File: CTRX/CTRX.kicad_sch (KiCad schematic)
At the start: 3 parts, among them J1 USB_B_Micro, U1 nRF52820-QDxx, U2 NRF21540-QDAA-R7

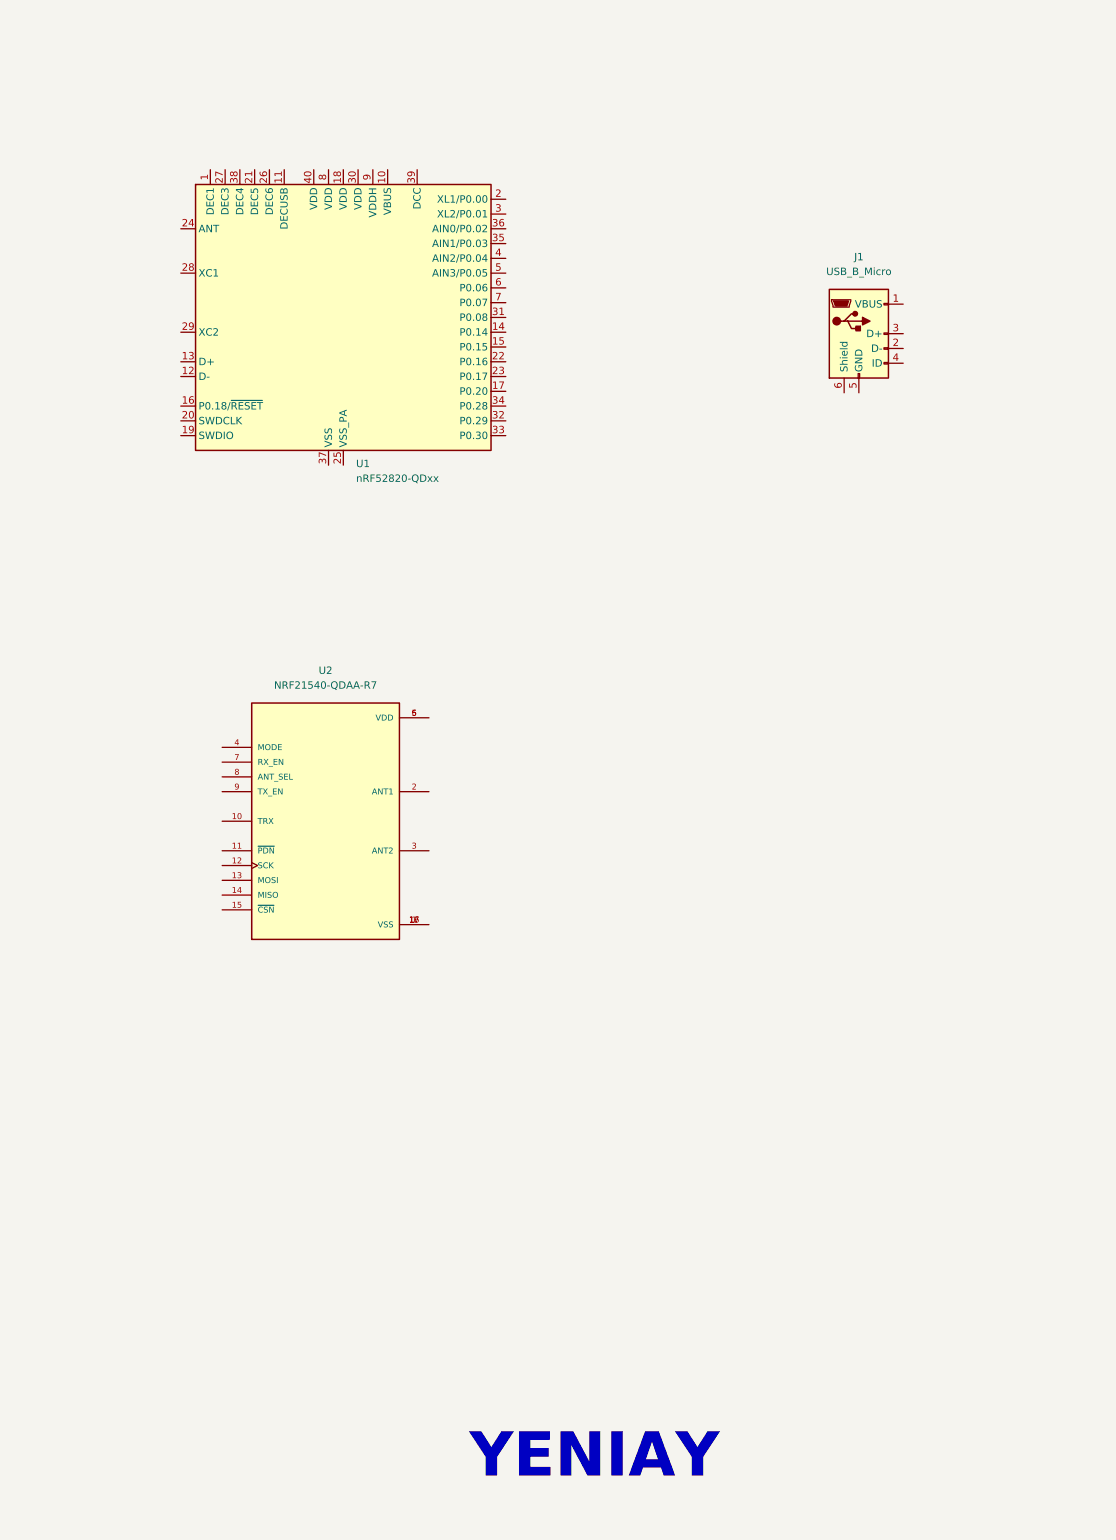
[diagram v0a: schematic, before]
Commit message: Selecting and adding component
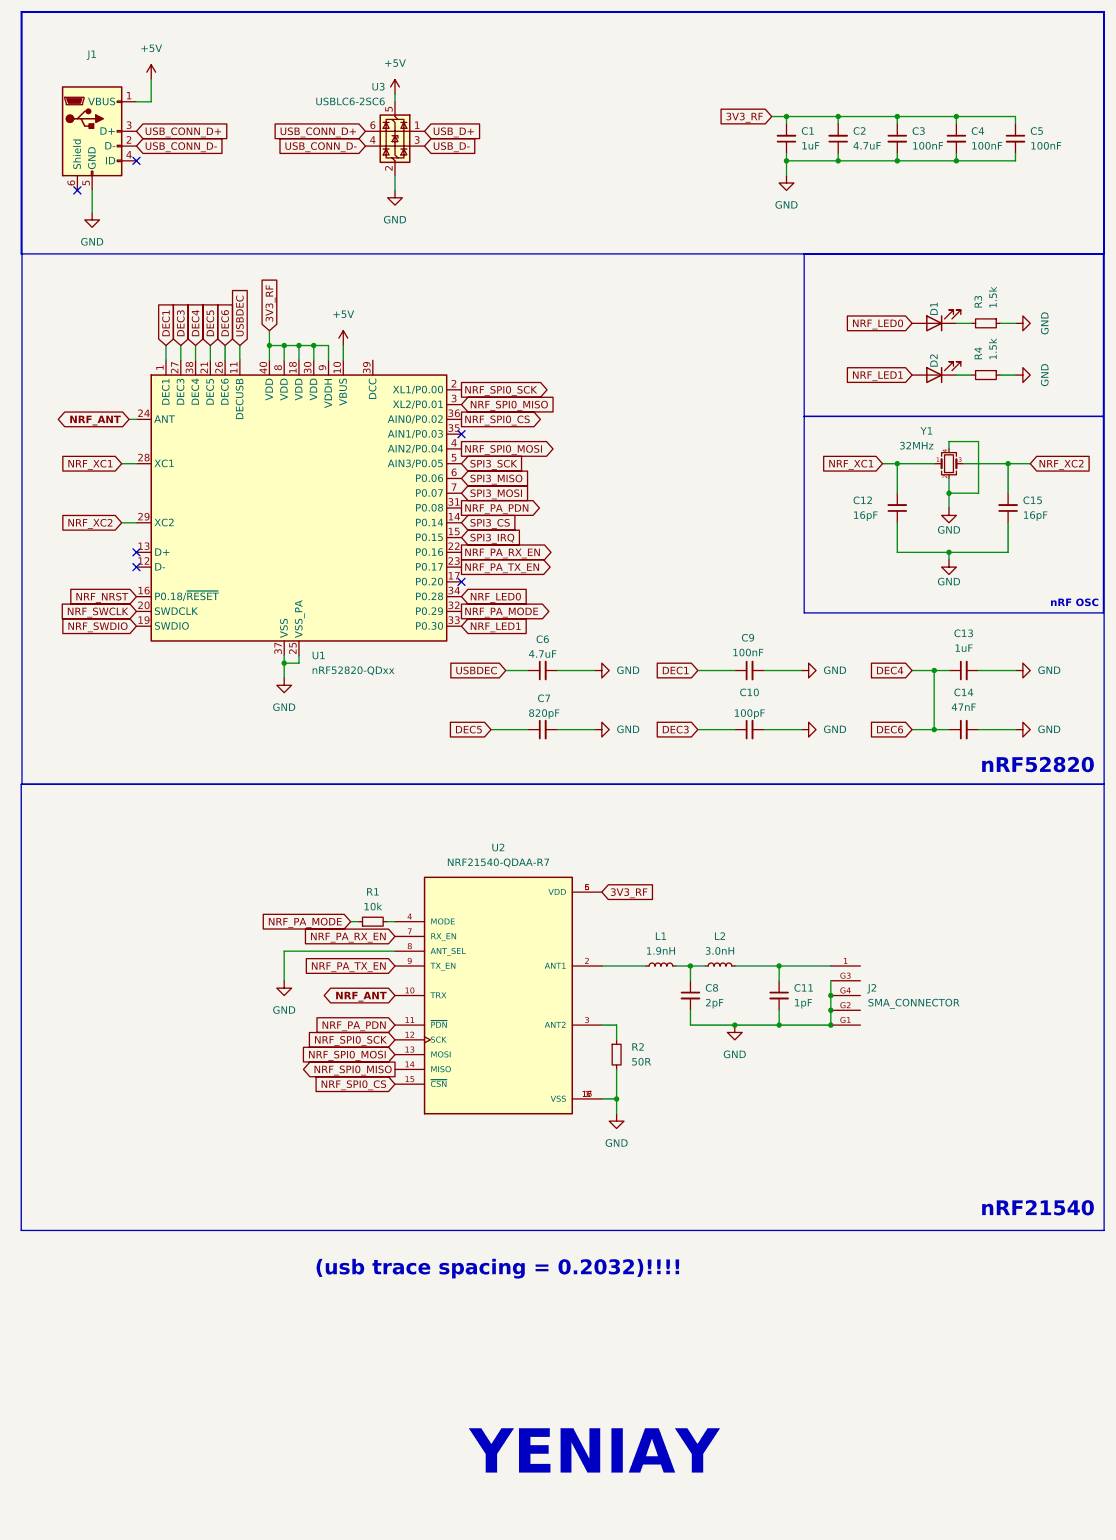
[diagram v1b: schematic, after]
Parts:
- added C1, C13: 1uF, Capacitor_SMD:C_0402_1005Metric, symbol Device:C_Small
- added C10: 100pF, Capacitor_SMD:C_0201_0603Metric, symbol Device:C_Small
- added C11: 1pF, Capacitor_SMD:C_0201_0603Metric, symbol Device:C_Small
- added C12, C15: 16pF, Capacitor_SMD:C_0201_0603Metric, symbol Device:C_Small
- added C14: 47nF, Capacitor_SMD:C_0201_0603Metric, symbol Device:C_Small
- added C2, C6: 4.7uF, Capacitor_SMD:C_0603_1608Metric, symbol Device:C_Small
- added C3, C4, C5, C9: 100nF, Capacitor_SMD:C_0201_0603Metric, symbol Device:C_Small
- added C7: 820pF, Capacitor_SMD:C_0201_0603Metric, symbol Device:C_Small
- added C8: 2pF, Capacitor_SMD:C_0201_0603Metric, symbol Device:C_Small
- added D1, D2: LED, LED_SMD:LED_0402_1005Metric, symbol Device:LED
- added J2: SMA_CONNECTOR, LPRS_SMA_CONNECTOR:LPRS_SMA_CONNECTOR, symbol SMA_CONNECTOR:SMA_CONNECTOR
- added L1: 1.9nH, Inductor_SMD:L_0201_0603Metric, symbol Device:L_Small
- added L2: 3.0nH, Inductor_SMD:L_0201_0603Metric, symbol Device:L_Small
- added R1: 10k, Resistor_SMD:R_0402_1005Metric, symbol Device:R_Small
- added R2: 50R, Resistor_SMD:R_0402_1005Metric, symbol Device:R_Small
- added R3, R4: 1.5k, Resistor_SMD:R_0402_1005Metric, symbol Device:R_Small
- added U3: USBLC6-2SC6, Package_TO_SOT_SMD:SOT-23-6, symbol Power_Protection:USBLC6-2SC6
- added Y1: 32MHz, Crystal:Crystal_SMD_3225-4Pin_3.2x2.5mm, symbol Device:Crystal_GND24_Small
- U2: footprint NRF21540-QDAA-R7:QFN65P400X400X95-17N -> nRF21540:QFN65P400X400X95-17N
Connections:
- net +5V: now reaches J1.1 (VBUS)
- net +5V: now also U1.10 (VBUS), U3.5 (VBUS)
- net USB_CONN_D-: now reaches J1.2 (D-)
- net USB_CONN_D-: now also U3.4 (I/O2)
- net USB_CONN_D+: now reaches J1.3 (D+)
- net USB_CONN_D+: now also U3.6 (I/O1)
- net GND: now reaches J1.5 (GND)
- net GND: now also U1.25 (VSS_PA), U1.37 (VSS), U1.41 (VSS), U2.1 (VSS), U2.16 (VSS), U2.17 (VSS), U2.8 (ANT_SEL), C1.1, C10.2, C11.2, C12.1, C13.2, C14.2, C15.1, C2.1, C3.2, C4.2, C5.2, C6.2, C7.2, C8.2, C9.2, J2.G1, J2.G2, J2.G3, J2.G4, R2.2, R3.1, R4.1, U3.2 (GND), Y1.2, Y1.4
- net NRF_ANT: now reaches U2.10 (TRX)
- net NRF_ANT: now also U1.24 (ANT)
- net NRF_PA_PDN: now reaches U2.11 (~{PDN})
- net NRF_PA_PDN: now also U1.31 (P0.08)
- net NRF_SPI0_SCK: now reaches U2.12 (SCK)
- net NRF_SPI0_SCK: now also U1.2 (XL1/P0.00)
- net NRF_SPI0_MOSI: now reaches U2.13 (MOSI)
- net NRF_SPI0_MOSI: now also U1.4 (AIN2/P0.04)
- net NRF_SPI0_MISO: now reaches U2.14 (MISO)
- net NRF_SPI0_MISO: now also U1.3 (XL2/P0.01)
- net NRF_SPI0_CS: now reaches U2.15 (~{CSN})
- net NRF_SPI0_CS: now also U1.36 (AIN0/P0.02)
- net at U2.2 (ANT1): now also L1.1
- net at U2.3 (ANT2): now also R2.1
- net at U2.4 (MODE): now also R1.2
- net 3V3_RF: now reaches U2.5 (VDD), U2.6 (VDD)
- net 3V3_RF: now also U1.18 (VDD), U1.30 (VDD), U1.40 (VDD), U1.8 (VDD), U1.9 (VDDH), C1.2, C2.2, C3.1, C4.1, C5.1
- net NRF_PA_RX_EN: now reaches U2.7 (RX_EN)
- net NRF_PA_RX_EN: now also U1.22 (P0.16)
- net NRF_PA_TX_EN: now reaches U2.9 (TX_EN)
- net NRF_PA_TX_EN: now also U1.23 (P0.17)
- net DEC1: now reaches U1.1 (DEC1)
- net DEC1: now also C9.1
- net USBDEC: now reaches U1.11 (DECUSB)
- net USBDEC: now also C6.1
- net SPI3_CS: now reaches U1.14 (P0.14)
- net SPI3_IRQ: now reaches U1.15 (P0.15)
- net NRF_NRST: now reaches U1.16 (P0.18/~{RESET})
- net NRF_SWDIO: now reaches U1.19 (SWDIO)
- net NRF_SWCLK: now reaches U1.20 (SWDCLK)
- net DEC5: now reaches U1.21 (DEC5)
- net DEC5: now also C7.1
- net DEC4: now reaches U1.26 (DEC6)
- net DEC4: now also U1.38 (DEC4), C13.1, C14.1
- net DEC3: now reaches U1.27 (DEC3)
- net DEC3: now also C10.1
- net NRF_XC1: now reaches U1.28 (XC1)
- net NRF_XC1: now also C12.2, Y1.1
- net NRF_XC2: now reaches U1.29 (XC2)
- net NRF_XC2: now also C15.2, Y1.3
- net NRF_PA_MODE: now reaches U1.32 (P0.29)
- net NRF_PA_MODE: now also R1.1
- net NRF_LED1: now reaches U1.33 (P0.30)
- net NRF_LED1: now also D2.2 (A)
- net NRF_LED0: now reaches U1.34 (P0.28)
- net NRF_LED0: now also D1.2 (A)
- net SPI3_SCK: now reaches U1.5 (AIN3/P0.05)
- net SPI3_MISO: now reaches U1.6 (P0.06)
- net SPI3_MOSI: now reaches U1.7 (P0.07)
- new net: D1.1 (K), R3.2
- new net: C11.1, J2.1, L2.2
- new net: C8.1, L1.2, L2.1
- new net: D2.1 (K), R4.2
- new net USB_D+: U3.1 (I/O1)
- new net USB_D-: U3.3 (I/O2)
- no-connect marks 0 -> 6
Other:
- note added: "(usb trace spacing = 0.2032)!!!!"
- note added: "nRF OSC"
- note added: "nRF21540"
- note added: "nRF52820"
- moved on the sheet: J1

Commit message: Scheme drawing.
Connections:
- net 3V3_RF: no longer C1.2, C2.2, C3.1, C4.1, C5.1, U1.18 (VDD), U1.30 (VDD), U1.40 (VDD), U1.8 (VDD), U1.9 (VDDH)
- new net VDD_nRF: C1.2, C2.2, C3.1, C4.1, C5.1, U1.18 (VDD), U1.30 (VDD), U1.40 (VDD), U1.8 (VDD), U1.9 (VDDH)
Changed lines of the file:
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@@
 	(wire
 		(pts
-			(xy 77.47 41.91) (xy 77.47 44.45)
+			(xy 77.47 41.91) (xy 77.47 43.18)
 		)
 		(stroke
@@
 	)
 	(rectangle
-		(start 13.208 13.716)
+		(start 13.97 13.716)
 		(end 199.39 55.372)
 		(stroke
@@
 		)
 	)
-	(global_label "3V3_RF"
+	(global_label "VDD_nRF"
 		(shape input)
 		(at 142.24 31.75 180)
@@
 		)
 		(property "Intersheetrefs" "${INTERSHEET_REFS}"
-			(at 132.421 31.75 0)
+			(at 131.151 31.75 0)
 			(effects
 				(font
@@
 		)
 	)
+	(global_label "VDD_nRF"
+		(shape input)
+		(at 55.88 68.58 90)
+		(fields_autoplaced yes)
+		(effects
+			(font
+				(size 1.27 1.27)
+			)
+			(justify left)
+		)
+		(property "Intersheetrefs" "${INTERSHEET_REFS}"
+			(at 55.88 57.491 90)
+			(effects
+				(font
+					(size 1.27 1.27)
+				)
+				(justify left)
+				(hide yes)
+			)
+		)
+	)
 	(global_label "USB_D+"
 		(shape input)
@@
 		)
 	)
-	(global_label "3V3_RF"
-		(shape input)
-		(at 55.88 68.58 90)
-		(fields_autoplaced yes)
-		(effects
-			(font
-				(size 1.27 1.27)
-			)
-			(justify left)
-		)
-		(property "Intersheetrefs" "${INTERSHEET_REFS}"
-			(at 55.88 58.761 90)
-			(effects
-				(font
-					(size 1.27 1.27)
-				)
-				(justify left)
-				(hide yes)
-			)
-		)
-	)
 	(global_label "NRF_PA_MODE"
 		(shape output)
@@
 	(symbol
 		(lib_id "power:GND")
-		(at 77.47 44.45 0)
+		(at 77.47 43.18 0)
 		(unit 1)
 		(exclude_from_sim no)
@@
 		(fields_autoplaced yes)
 		(property "Reference" "#PWR019"
-			(at 77.47 50.8 0)
+			(at 77.47 49.53 0)
 			(effects
 				(font
@@
 		)
 		(property "Value" "GND"
-			(at 77.47 49.53 0)
+			(at 77.47 48.26 0)
 			(effects
 				(font
@@
 		)
 		(property "Footprint" ""
-			(at 77.47 44.45 0)
+			(at 77.47 43.18 0)
 			(effects
 				(font
@@
 		)
 		(property "Datasheet" ""
-			(at 77.47 44.45 0)
+			(at 77.47 43.18 0)
 			(effects
 				(font
@@
 		)
 		(property "Description" "Power symbol creates a global label with name \"GND\" , ground"
-			(at 77.47 44.45 0)
+			(at 77.47 43.18 0)
 			(effects
 				(font

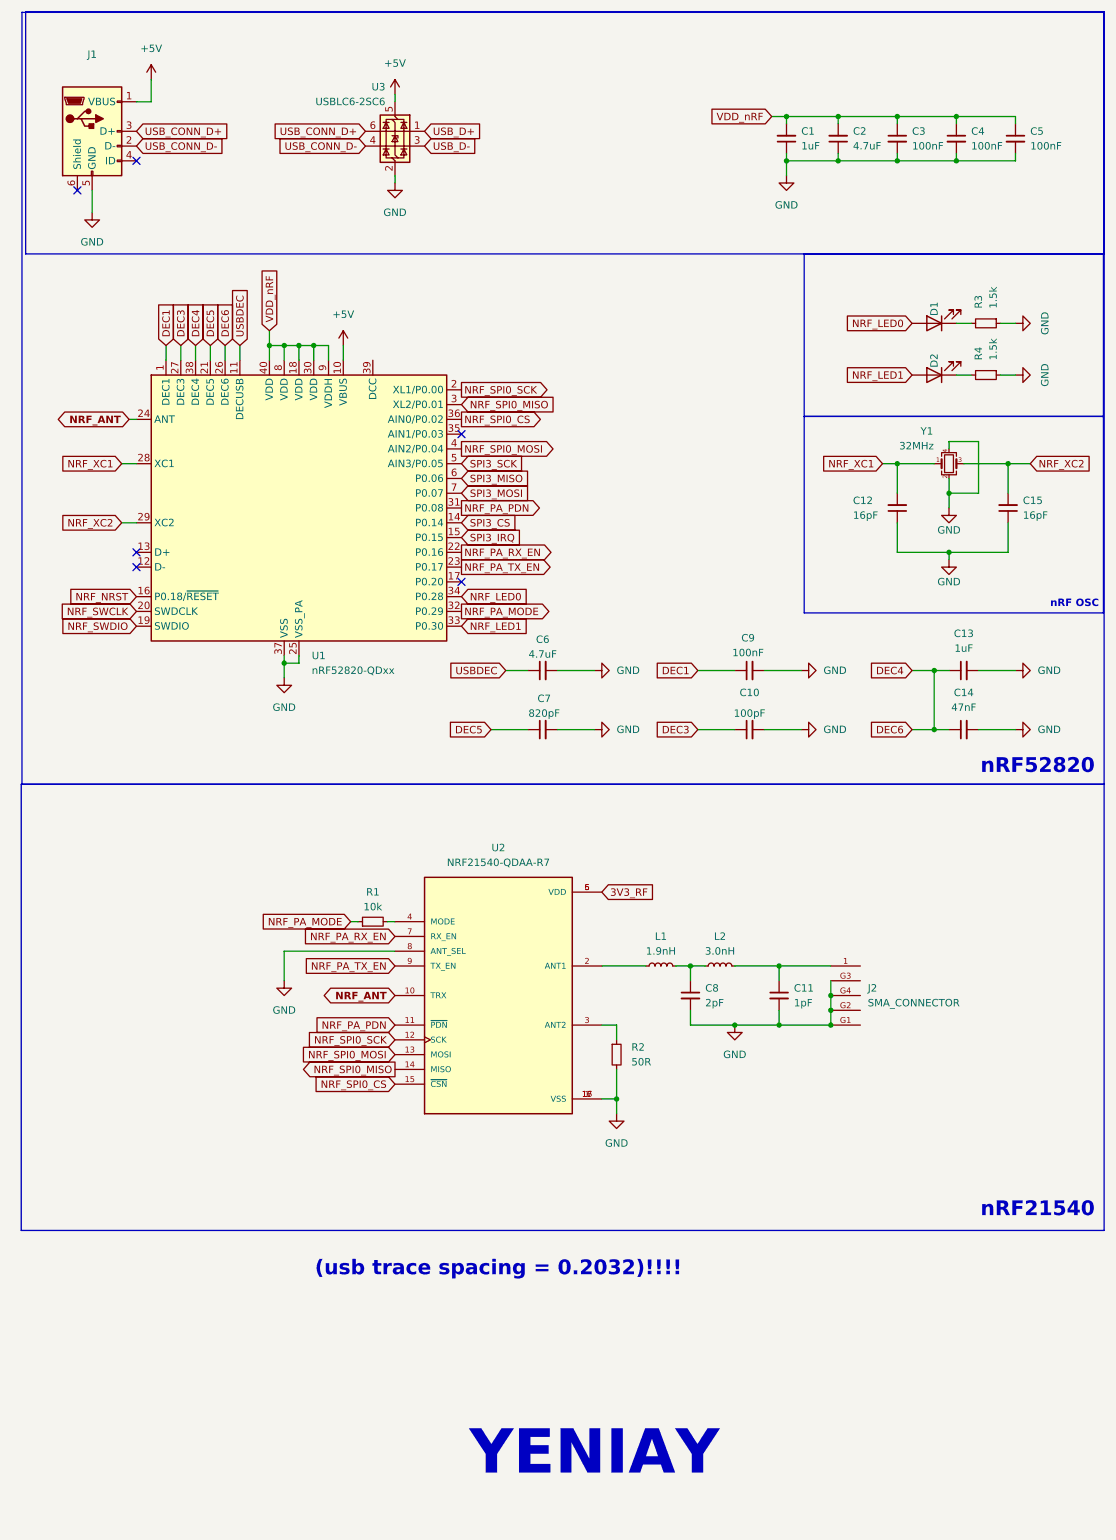
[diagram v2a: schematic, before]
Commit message: SPI3 pinleri kaldirildi, D+/D- baglantilari yapildi, NC pinler isaretlendi, C12/C15 12pF yapildi, dec kapasitorleri konumlandirildi, (2x5) debug connector ve ME6211 regulator eklendi.
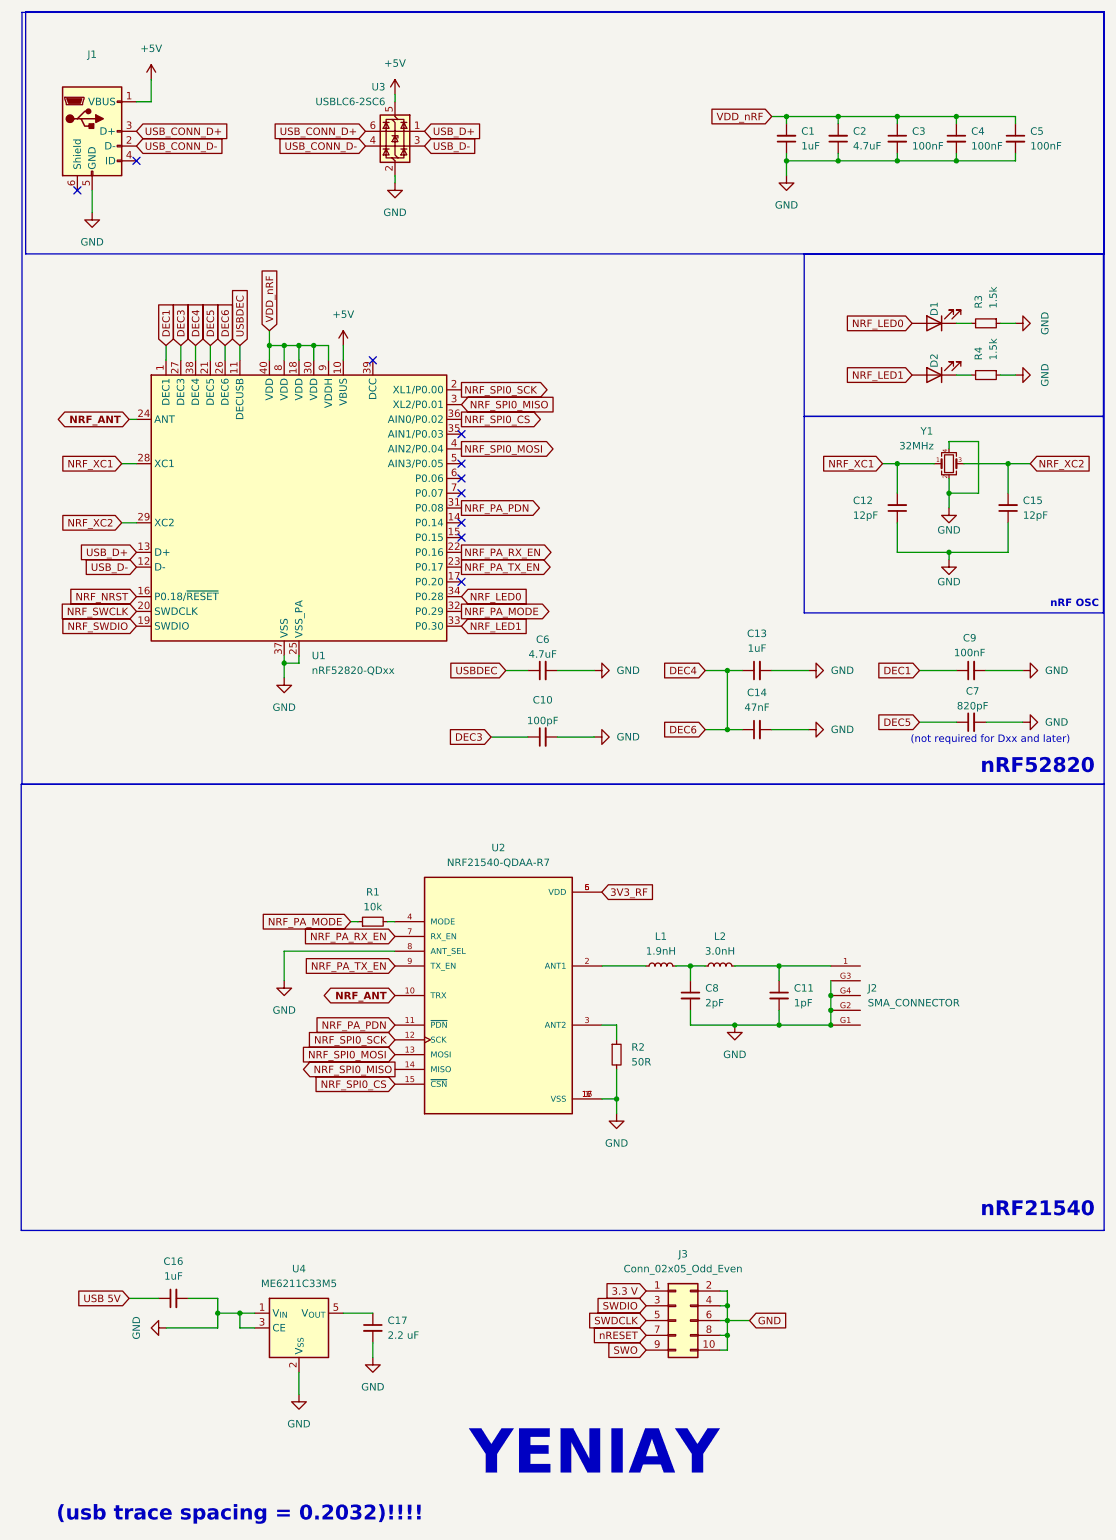
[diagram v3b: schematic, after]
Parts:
- added C16: 1uF, symbol Device:C_Small
- added C17: 2.2 uF, symbol Device:C_Small
- added J3: Conn_02x05_Odd_Even, symbol Connector_Generic:Conn_02x05_Odd_Even
- added U4: ME6211C33M5, Package_TO_SOT_SMD:SOT-23-5, symbol Regulator_Linear:ME6211C33M5
- C12, C15: value 16pF -> 12pF
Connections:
- net GND: now also C16.2, C17.2, J3.10 (Pin_10), J3.2 (Pin_2), J3.4 (Pin_4), J3.6 (Pin_6), J3.8 (Pin_8), U4.1 (V_{IN}), U4.2 (V_{SS}), U4.3 (CE)
- net USB_D+: now also U1.13 (D+)
- net USB_D-: now also U1.12 (D-)
- net SPI3_CS: no longer names the net of U1.14 (P0.14)
- net SPI3_IRQ: no longer names the net of U1.15 (P0.15)
- net SPI3_MISO: no longer names the net of U1.6 (P0.06)
- net SPI3_MOSI: no longer names the net of U1.7 (P0.07)
- net SPI3_SCK: no longer names the net of U1.5 (AIN3/P0.05)
- new net: C17.1, U4.5 (V_{OUT})
- new net 3.3 V: J3.1 (Pin_1)
- new net SWDCLK: J3.5 (Pin_5)
- new net SWDIO: J3.3 (Pin_3)
- new net SWO: J3.9 (Pin_9)
- new net USB 5V: C16.1
- new net nRESET: J3.7 (Pin_7)
- no-connect marks 6 -> 10
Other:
- note added: "(not required for Dxx and later)"
- moved on the sheet: C10, C13, C14, C7, C9
